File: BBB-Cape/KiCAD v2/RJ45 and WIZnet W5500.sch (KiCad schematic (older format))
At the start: 41 parts, among them J11 RJ45-TRANSFO, U2 WIZnet W5500, Y1 25MHz

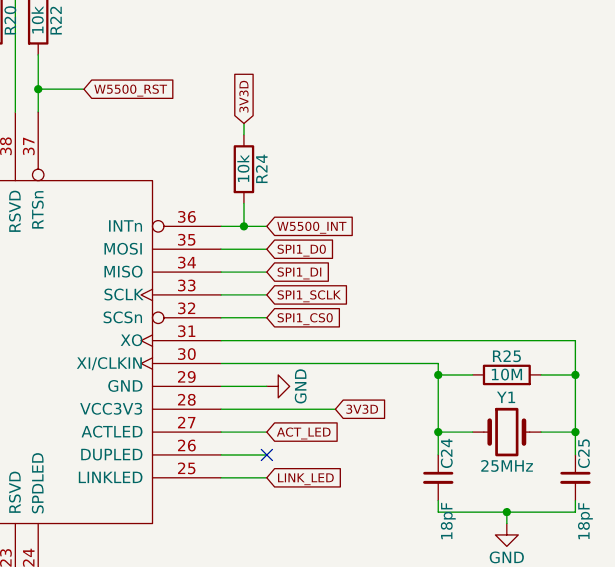
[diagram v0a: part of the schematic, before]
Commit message: Schematic Update
Updated pin mapping as described by Ed.
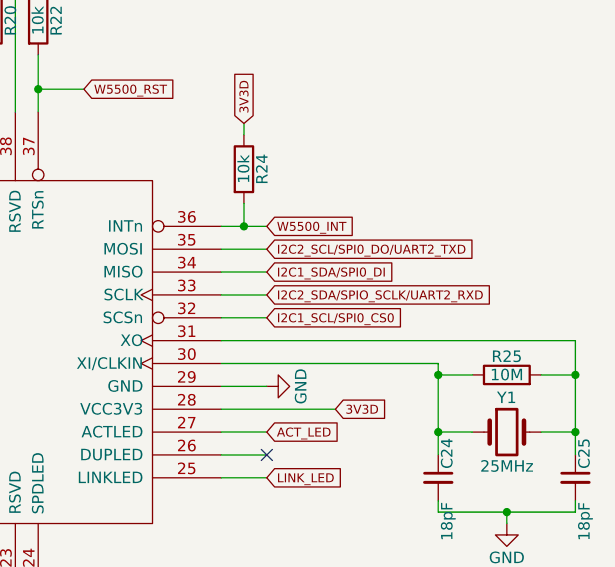
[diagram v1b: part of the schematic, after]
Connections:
- net SPI1_CS0 renamed I2C1_SCL/SPI0_CS0
- net SPI1_D0 renamed I2C2_SCL/SPI0_DO/UART2_TXD
- net SPI1_DI renamed I2C1_SDA/SPI0_DI
- net SPI1_SCLK renamed I2C2_SDA/SPIO_SCLK/UART2_RXD
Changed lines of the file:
@@
 	1    0    0    -1
 $EndComp
-Text GLabel 8250 2500 2    39   Input ~ 0
-SPI1_DI
-Text GLabel 8250 2400 2    39   Input ~ 0
-SPI1_D0
-Text GLabel 8250 2600 2    39   Input ~ 0
-SPI1_SCLK
-Text GLabel 8250 2700 2    39   Input ~ 0
-SPI1_CS0
 Text Notes 7500 5200 2    39   ~ 0
 Keep Trace Short as possible on \nC10 to stabilize internals\n
@@
 	8050 2500 8250 2500
 Wire Wire Line
-	8050 2600 8250 2600
-Wire Wire Line
 	8050 2700 8250 2700
 Wire Wire Line
@@
 	8150 2200 8150 2300
 Connection ~ 8150 2300
+Text GLabel 8250 2700 2    39   Input ~ 0
+I2C1_SCL/SPI0_CS0
+Text GLabel 8250 2400 2    39   Input ~ 0
+I2C2_SCL/SPI0_DO/UART2_TXD
+Text GLabel 8250 2500 2    39   Input ~ 0
+I2C1_SDA/SPI0_DI
+Wire Wire Line
+	8050 2600 8250 2600
+Text GLabel 8250 2600 2    39   Input ~ 0
+I2C2_SDA/SPIO_SCLK/UART2_RXD
 $EndSCHEMATC

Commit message: Layout Update
Changed RJ45 connector to a surface mount component. Need to properly reposition P8 and P9.
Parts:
- J11: footprint Connectors:RJ45_TRANSFO -> RJ45:RJ45_Surface_Mount
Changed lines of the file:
@@
 F 0 "J11" H 1600 6100 50  0000 L CNN
 F 1 "RJ45-TRANSFO" H 1450 6100 50  0000 R CNN
-F 2 "Connectors:RJ45_TRANSFO" H 1500 5500 50  0001 C CNN
+F 2 "RJ45:RJ45_Surface_Mount" H 1500 5500 50  0001 C CNN
 F 3 "" H 1500 5500 50  0001 C CNN
 	1    1500 5500
